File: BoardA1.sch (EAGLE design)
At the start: 19 parts, among them J1 LOAD_CELL1X03-PTH, J2 FEMALE 2x3, J3 LOAD_CELL1X03-PTH, J5 LOAD_CELL1X03-PTH, J6 LOAD_CELL1X03-PTH

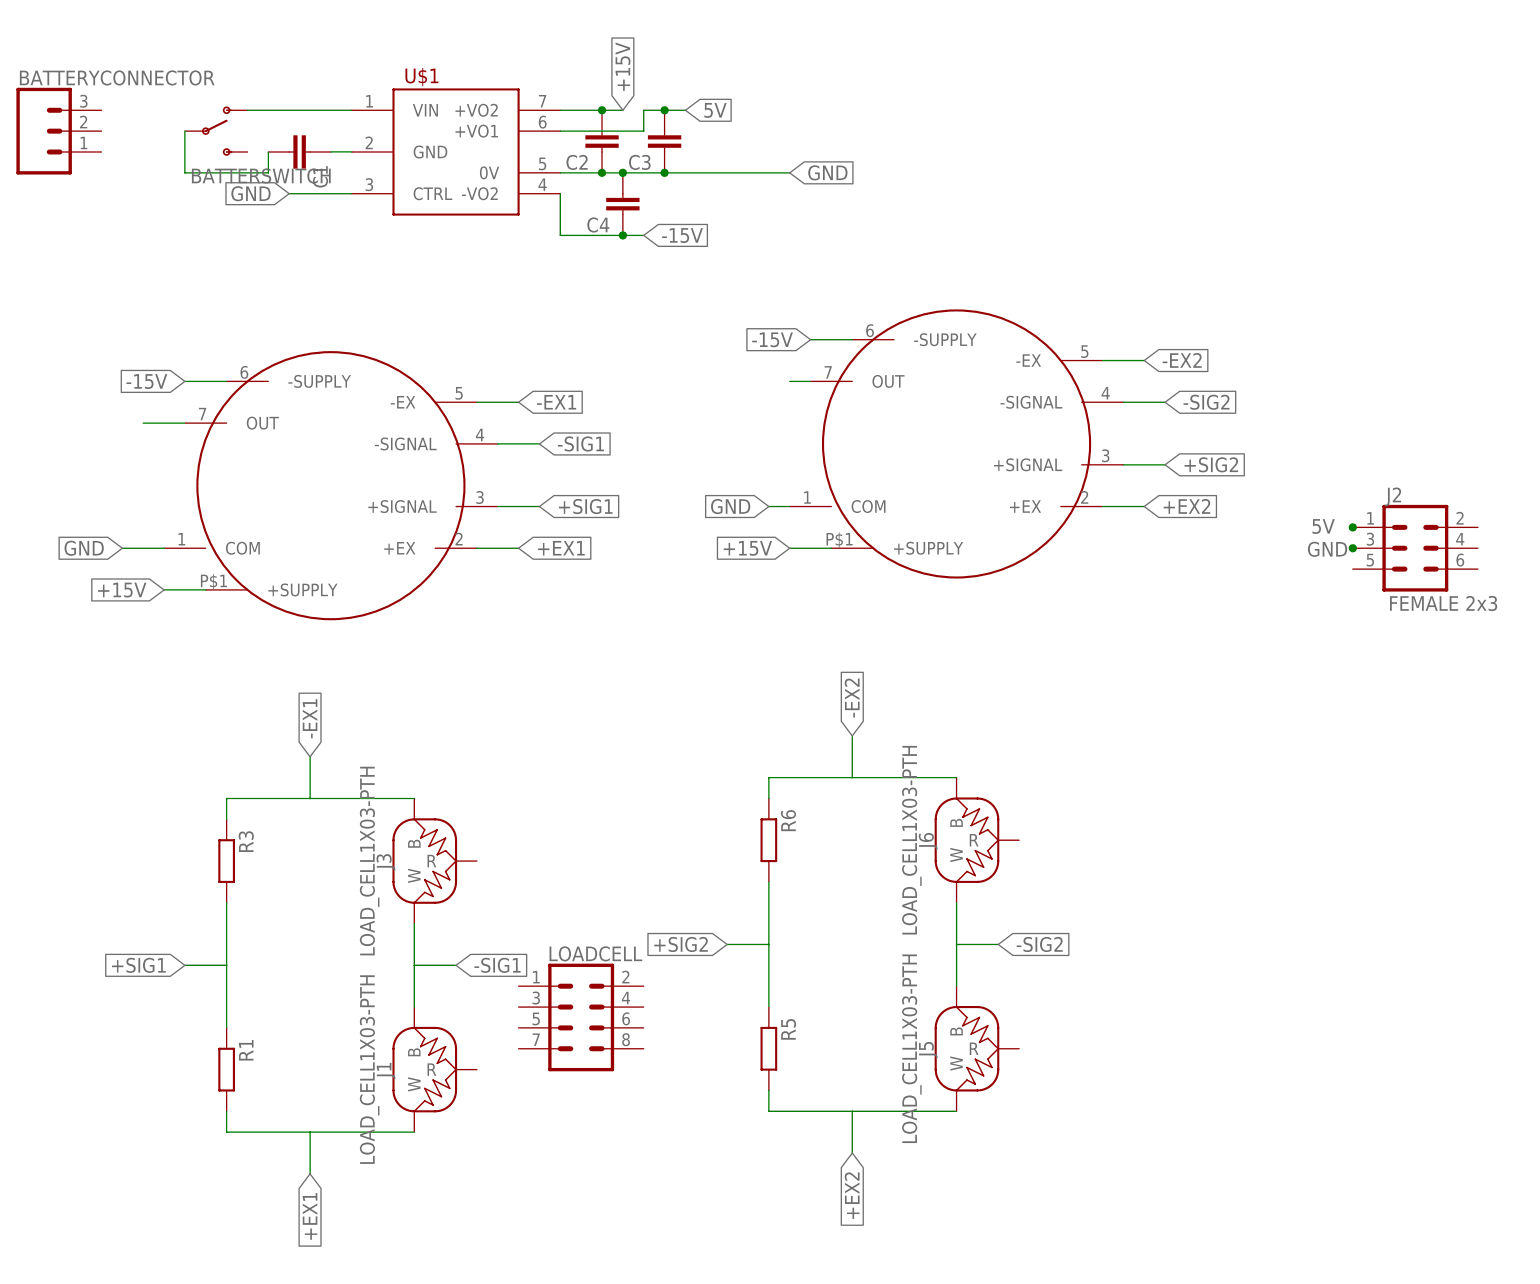
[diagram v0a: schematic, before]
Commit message: Connections on Power board
- hook up the load cell connectors
- ch1 and ch2 connection to the middle board
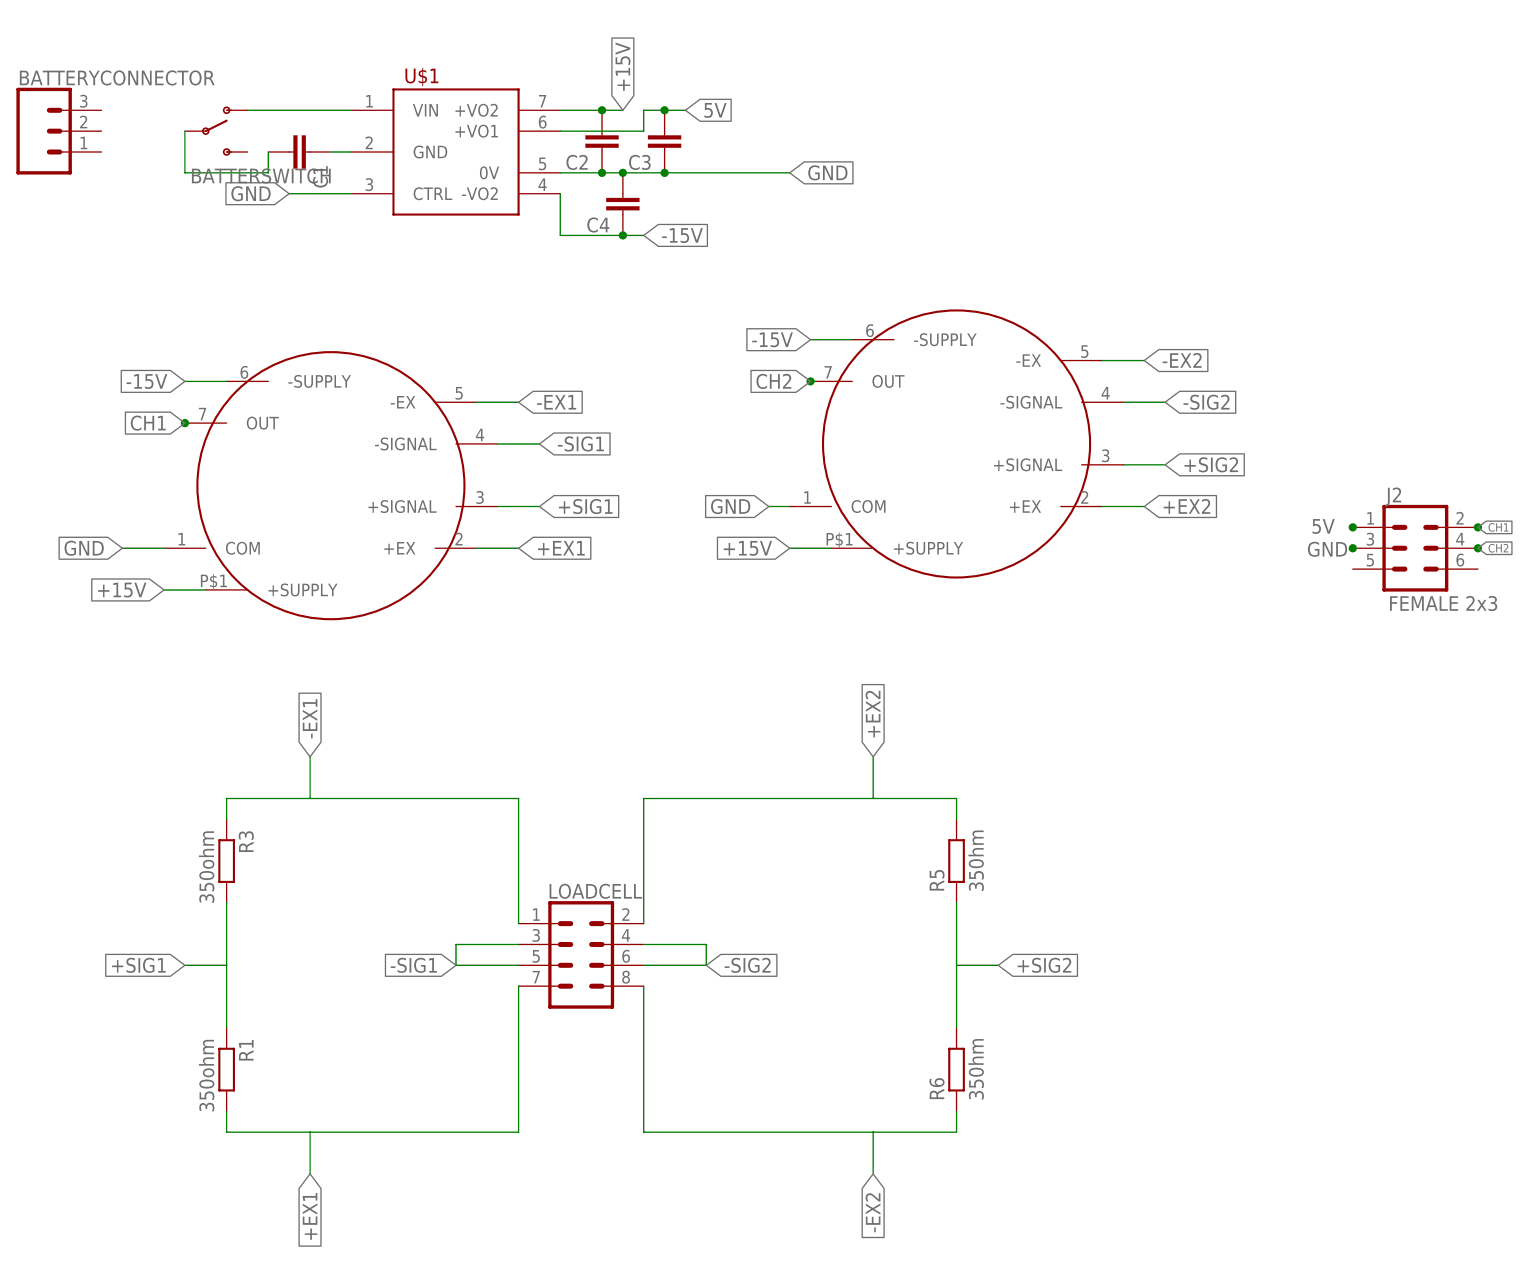
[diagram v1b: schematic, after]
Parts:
- removed J1, J3, J5, J6: LOAD_CELL1X03-PTH, Smartcrutches:LOAD_CELL1X03-PTH
- R1, R3: value (none) -> 350ohm
- R5, R6: value (none) -> 350hm
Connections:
- removed net N$4: U$3.OUT
- removed net N$5: U$2.OUT
- new net CH1: J2.2, U$2.OUT
- new net CH2: J2.4, U$3.OUT
- net +EX1: now also LOADCELL.7; no longer J1.W
- net +EX2: now also LOADCELL.2; no longer J5.W
- net -EX1: now also LOADCELL.1; no longer J3.B
- net -EX2: now also LOADCELL.8; no longer J6.B
- net -SIG1: now also LOADCELL.3, LOADCELL.5; no longer J1.B, J3.W
- net -SIG2: now also LOADCELL.4, LOADCELL.6; no longer J5.B, J6.W
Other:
- moved on the sheet: LOADCELL, R5, R6

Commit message: Routing1
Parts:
- renumbered U$2 to UPP_LC_AMP1, U$3 to UPP_LC_AMP2
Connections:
- net CH1: now also J2.4; no longer J2.2
- net CH2: now also J2.2; no longer J2.4
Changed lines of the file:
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@@
 <part name="C3" library="SparkFun-Capacitors" deviceset="CAP" device="KIT"/>
 <part name="C4" library="SparkFun-Capacitors" deviceset="CAP" device="KIT"/>
-<part name="U$2" library="Smartcrutches" deviceset="ICA3H" device=""/>
+<part name="UPP_LC_AMP1" library="Smartcrutches" deviceset="ICA3H" device=""/>
 <part name="R1" library="eagle-ltspice" library_urn="urn:adsk.eagle:library:217" deviceset="R" device="0204/7" value="350ohm"/>
 <part name="R3" library="eagle-ltspice" library_urn="urn:adsk.eagle:library:217" deviceset="R" device="0204/7" value="350ohm"/>
-<part name="U$3" library="Smartcrutches" deviceset="ICA3H" device=""/>
+<part name="UPP_LC_AMP2" library="Smartcrutches" deviceset="ICA3H" device=""/>
 <part name="R5" library="eagle-ltspice" library_urn="urn:adsk.eagle:library:217" deviceset="R" device="0204/7" value="350hm"/>
 <part name="R6" library="eagle-ltspice" library_urn="urn:adsk.eagle:library:217" deviceset="R" device="0204/7" value="350hm"/>
@@
 <instance part="C3" gate="G$1" x="43.18" y="53.34" rot="R180"/>
 <instance part="C4" gate="G$1" x="38.1" y="45.72" rot="R180"/>
-<instance part="U$2" gate="G$1" x="2.54" y="10.16"/>
+<instance part="UPP_LC_AMP1" gate="G$1" x="2.54" y="10.16"/>
 <instance part="R1" gate="G$1" x="-10.16" y="-60.96" rot="R270"/>
 <instance part="R3" gate="G$1" x="-10.16" y="-35.56" rot="R270"/>
-<instance part="U$3" gate="G$1" x="78.74" y="15.24"/>
+<instance part="UPP_LC_AMP2" gate="G$1" x="78.74" y="15.24"/>
 <instance part="R5" gate="G$1" x="78.74" y="-35.56" rot="R90"/>
 <instance part="R6" gate="G$1" x="78.74" y="-60.96" rot="R90"/>
@@
 </segment>
 <segment>
-<pinref part="U$2" gate="G$1" pin="COM"/>
+<pinref part="UPP_LC_AMP1" gate="G$1" pin="COM"/>
 <wire x1="-17.78" y1="2.54" x2="-22.86" y2="2.54" width="0.1524" layer="91"/>
 <label x="-22.86" y="2.54" size="1.778" layer="95" rot="R180" xref="yes"/>
 </segment>
 <segment>
-<pinref part="U$3" gate="G$1" pin="COM"/>
+<pinref part="UPP_LC_AMP2" gate="G$1" pin="COM"/>
 <wire x1="58.42" y1="7.62" x2="55.88" y2="7.62" width="0.1524" layer="91"/>
 <label x="55.88" y="7.62" size="1.778" layer="95" rot="R180" xref="yes"/>
@@
 </segment>
 <segment>
-<pinref part="U$2" gate="G$1" pin="+SUPPLY"/>
+<pinref part="UPP_LC_AMP1" gate="G$1" pin="+SUPPLY"/>
 <wire x1="-12.7" y1="-2.54" x2="-17.78" y2="-2.54" width="0.1524" layer="91"/>
 <label x="-17.78" y="-2.54" size="1.778" layer="95" rot="R180" xref="yes"/>
 </segment>
 <segment>
-<pinref part="U$3" gate="G$1" pin="+SUPPLY"/>
+<pinref part="UPP_LC_AMP2" gate="G$1" pin="+SUPPLY"/>
 <wire x1="63.5" y1="2.54" x2="58.42" y2="2.54" width="0.1524" layer="91"/>
 <label x="58.42" y="2.54" size="1.778" layer="95" rot="R180" xref="yes"/>
@@
 </segment>
 <segment>
-<pinref part="U$2" gate="G$1" pin="-SUPPLY"/>
+<pinref part="UPP_LC_AMP1" gate="G$1" pin="-SUPPLY"/>
 <wire x1="-10.16" y1="22.86" x2="-15.24" y2="22.86" width="0.1524" layer="91"/>
 <label x="-15.24" y="22.86" size="1.778" layer="95" rot="R180" xref="yes"/>
 </segment>
 <segment>
-<pinref part="U$3" gate="G$1" pin="-SUPPLY"/>
+<pinref part="UPP_LC_AMP2" gate="G$1" pin="-SUPPLY"/>
 <wire x1="66.04" y1="27.94" x2="60.96" y2="27.94" width="0.1524" layer="91"/>
 <label x="60.96" y="27.94" size="1.778" layer="95" rot="R180" xref="yes"/>
@@
 <net name="-EX1" class="0">
 <segment>
-<pinref part="U$2" gate="G$1" pin="-EX"/>
+<pinref part="UPP_LC_AMP1" gate="G$1" pin="-EX"/>
 <wire x1="20.32" y1="20.32" x2="25.4" y2="20.32" width="0.1524" layer="91"/>
 <label x="25.4" y="20.32" size="1.778" layer="95" xref="yes"/>
@@
 <net name="-SIG1" class="0">
 <segment>
-<pinref part="U$2" gate="G$1" pin="-SIGNAL"/>
+<pinref part="UPP_LC_AMP1" gate="G$1" pin="-SIGNAL"/>
 <wire x1="22.86" y1="15.24" x2="27.94" y2="15.24" width="0.1524" layer="91"/>
 <label x="27.94" y="15.24" size="1.778" layer="95" xref="yes"/>
@@
 <net name="+SIG1" class="0">
 <segment>
-<pinref part="U$2" gate="G$1" pin="+SIGNAL"/>
+<pinref part="UPP_LC_AMP1" gate="G$1" pin="+SIGNAL"/>
 <wire x1="22.86" y1="7.62" x2="27.94" y2="7.62" width="0.1524" layer="91"/>
 <label x="27.94" y="7.62" size="1.778" layer="95" xref="yes"/>
@@
 <net name="+EX1" class="0">
 <segment>
-<pinref part="U$2" gate="G$1" pin="+EX"/>
+<pinref part="UPP_LC_AMP1" gate="G$1" pin="+EX"/>
 <wire x1="20.32" y1="2.54" x2="25.4" y2="2.54" width="0.1524" layer="91"/>
 <label x="25.4" y="2.54" size="1.778" layer="95" xref="yes"/>
@@
 <net name="-EX2" class="0">
 <segment>
-<pinref part="U$3" gate="G$1" pin="-EX"/>
+<pinref part="UPP_LC_AMP2" gate="G$1" pin="-EX"/>
 <wire x1="96.52" y1="25.4" x2="101.6" y2="25.4" width="0.1524" layer="91"/>
 <label x="101.6" y="25.4" size="1.778" layer="95" xref="yes"/>
@@
 <net name="-SIG2" class="0">
 <segment>
-<pinref part="U$3" gate="G$1" pin="-SIGNAL"/>
+<pinref part="UPP_LC_AMP2" gate="G$1" pin="-SIGNAL"/>
 <wire x1="99.06" y1="20.32" x2="104.14" y2="20.32" width="0.1524" layer="91"/>
 <label x="104.14" y="20.32" size="1.778" layer="95" xref="yes"/>
@@
 <net name="+SIG2" class="0">
 <segment>
-<pinref part="U$3" gate="G$1" pin="+SIGNAL"/>
+<pinref part="UPP_LC_AMP2" gate="G$1" pin="+SIGNAL"/>
 <wire x1="99.06" y1="12.7" x2="104.14" y2="12.7" width="0.1524" layer="91"/>
 <label x="104.14" y="12.7" size="1.778" layer="95" xref="yes"/>
@@
 <net name="+EX2" class="0">
 <segment>
-<pinref part="U$3" gate="G$1" pin="+EX"/>
+<pinref part="UPP_LC_AMP2" gate="G$1" pin="+EX"/>
 <wire x1="96.52" y1="7.62" x2="101.6" y2="7.62" width="0.1524" layer="91"/>
 <label x="101.6" y="7.62" size="1.778" layer="95" xref="yes"/>
@@
 <net name="CH1" class="0">
 <segment>
-<pinref part="U$2" gate="G$1" pin="OUT"/>
+<pinref part="UPP_LC_AMP1" gate="G$1" pin="OUT"/>
 <junction x="-15.24" y="17.78"/>
 <label x="-15.24" y="17.78" size="1.778" layer="95" rot="R180" xref="yes"/>
+</segment>
+<segment>
+<pinref part="J2" gate="G$1" pin="4"/>
+<junction x="142.24" y="2.54"/>
+<label x="142.24" y="2.54" size="1.016" layer="95" xref="yes"/>
+</segment>
+</net>
+<net name="CH2" class="0">
+<segment>
+<pinref part="UPP_LC_AMP2" gate="G$1" pin="OUT"/>
+<junction x="60.96" y="22.86"/>
+<label x="60.96" y="22.86" size="1.778" layer="95" rot="R180" xref="yes"/>
 </segment>
 <segment>
@@
 </segment>
 </net>
-<net name="CH2" class="0">
-<segment>
-<pinref part="U$3" gate="G$1" pin="OUT"/>
-<junction x="60.96" y="22.86"/>
-<label x="60.96" y="22.86" size="1.778" layer="95" rot="R180" xref="yes"/>
-</segment>
-<segment>
-<pinref part="J2" gate="G$1" pin="4"/>
-<junction x="142.24" y="2.54"/>
-<label x="142.24" y="2.54" size="1.016" layer="95" xref="yes"/>
-</segment>
-</net>
